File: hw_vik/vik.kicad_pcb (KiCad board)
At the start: 2 copper layers, 51.2 x 51.2 mm, 41 parts, among them J1 Conn_2Rows-05Pins, Q1 AO3401A, Q2 AO3401A, Q3 AO3401A, SW1 SW_DPST_x2, U1 PY32F002AF15P6TU

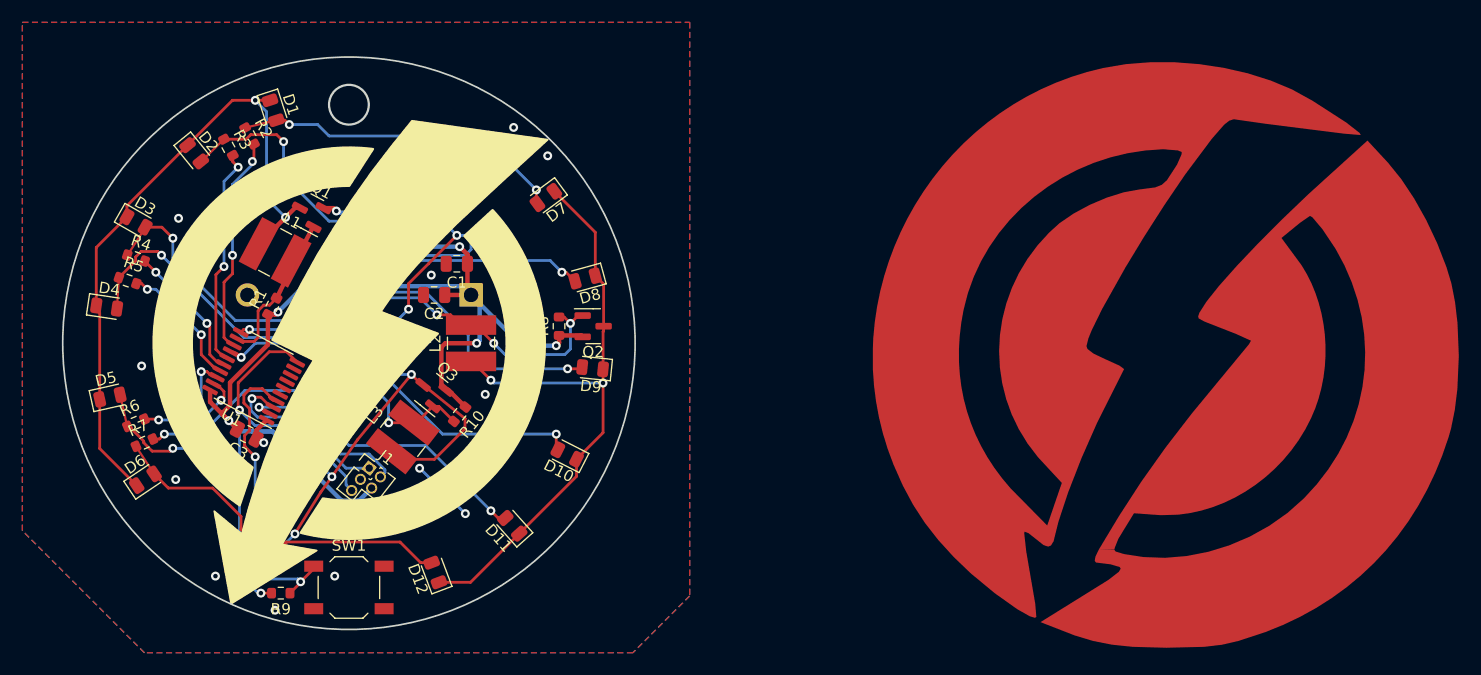
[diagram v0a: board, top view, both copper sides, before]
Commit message: Update pcb
Made FMask for exclude leds, added generated image
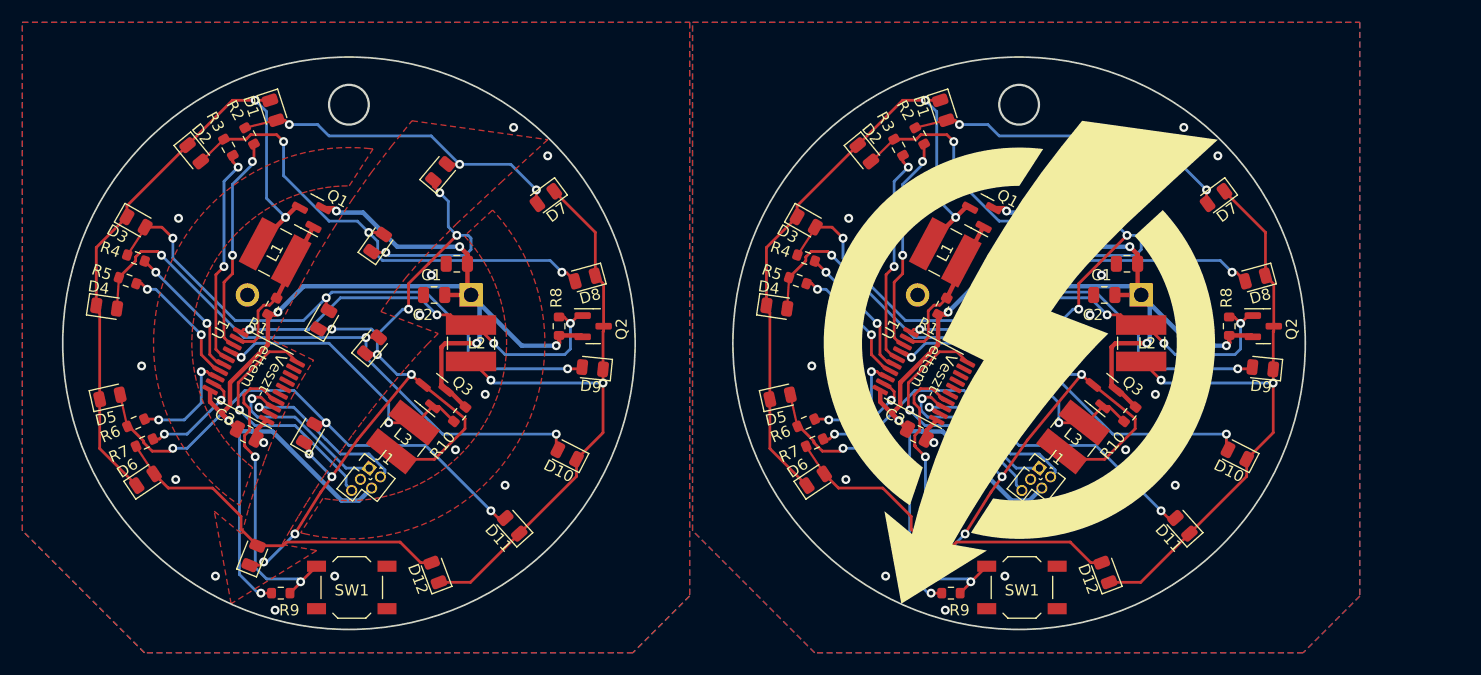
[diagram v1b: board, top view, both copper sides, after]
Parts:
- added BT1: CR2032, karifa:CR2032_Holder, B.Cu at (170.9, 95.7)
- added C1: 10uF, Capacitor_SMD:C_0805_2012Metric, F.Cu at (169.6, 92.9)
- added C2: 10uF, Capacitor_SMD:C_0805_2012Metric, F.Cu at (167.6, 95.7)
- added C3: 100nF, Capacitor_SMD:C_0805_2012Metric, F.Cu at (150.8, 108.1)
- added D1: LED, LED_SMD:LED_0805_2012Metric, F.Cu at (153.2, 79.2)
- added D10: LED, LED_SMD:LED_0805_2012Metric, F.Cu at (179.5, 110.0)
- added D11: LED, LED_SMD:LED_0805_2012Metric, F.Cu at (174.6, 116.3)
- added D12: LED, LED_SMD:LED_0805_2012Metric, F.Cu at (167.7, 120.5)
- added D13: LED, LED_SMD:LED_0805_2012Metric, F.Cu at (168.1, 84.7)
- added D14: LED, LED_SMD:LED_0805_2012Metric, F.Cu at (162.5, 91.0)
- added D15: LED, LED_SMD:LED_0805_2012Metric, F.Cu at (157.7, 97.9)
- added D16: LED, LED_SMD:LED_0805_2012Metric, F.Cu at (162.0, 100.2)
- added D17: LED, LED_SMD:LED_0805_2012Metric, F.Cu at (156.4, 108.1)
- added D18: LED, LED_SMD:LED_0805_2012Metric, F.Cu at (151.4, 119.0)
- added D2: LED, LED_SMD:LED_0805_2012Metric, F.Cu at (146.1, 83.0)
- added D3: LED, LED_SMD:LED_0805_2012Metric, F.Cu at (140.9, 89.2)
- added D4: LED, LED_SMD:LED_0805_2012Metric, F.Cu at (138.3, 96.8)
- added D5: LED, LED_SMD:LED_0805_2012Metric, F.Cu at (138.6, 104.8)
- added D6: LED, LED_SMD:LED_0805_2012Metric, F.Cu at (141.7, 112.2)
- added D7: LED, LED_SMD:LED_0805_2012Metric, F.Cu at (177.6, 87.0)
- added D8: LED, LED_SMD:LED_0805_2012Metric, F.Cu at (181.1, 94.2)
- added D9: LED, LED_SMD:LED_0805_2012Metric, F.Cu at (181.7, 102.2)
- added J1: Conn_2Rows-05Pins, karifa:ProgConnector_5pin, F.Cu at (161.8, 111.2)
- added L1: 1mH, Inductor_SMD:L_Ferrocore_DLG-0403, F.Cu at (153.3, 91.9)
- added L2: 1mH, Inductor_SMD:L_Ferrocore_DLG-0403, F.Cu at (170.9, 100.0)
- added L3: 1mH, Inductor_SMD:L_Ferrocore_DLG-0403, F.Cu at (164.8, 108.4)
- added Q1: AO3401A, karifa:SOT-23, F.Cu at (156.4, 88.3)
- added Q2: AO3401A, karifa:SOT-23, F.Cu at (181.8, 98.5)
- added Q3: AO3401A, karifa:SOT-23, F.Cu at (167.3, 104.3)
- added R1: 100k, Resistor_SMD:R_0603_1608Metric, F.Cu at (153.1, 96.7)
- added R10: 100k, Resistor_SMD:R_0603_1608Metric, F.Cu at (169.8, 106.3)
- added R2: 10, Resistor_SMD:R_0603_1608Metric, F.Cu at (151.1, 81.5)
- added R3: 10, Resistor_SMD:R_0603_1608Metric, F.Cu at (149.2, 82.5)
- added R4: 10, Resistor_SMD:R_0603_1608Metric, F.Cu at (140.9, 92.4)
- added R5: 10, Resistor_SMD:R_0603_1608Metric, F.Cu at (140.1, 94.4)
- added R6: 10, Resistor_SMD:R_0603_1608Metric, F.Cu at (140.9, 107.1)
- added R7: 10, Resistor_SMD:R_0603_1608Metric, F.Cu at (141.7, 108.9)
- added R8: 100k, Resistor_SMD:R_0603_1608Metric, F.Cu at (178.7, 98.5)
- added R9: 100k, Resistor_SMD:R_0603_1608Metric, F.Cu at (153.8, 122.4)
- added SW1: SW_DPST_x2, Button_Switch_SMD:SW_SPST_TL3342, F.Cu at (160.2, 121.8)
- added U1: PY32F002AF15P6TU, karifa:TSSOP-20_4.4x6.5mm_P0.65mm, F.Cu at (151.4, 102.9)
- moved SW1 0.25 mm to (100.3, 121.8)
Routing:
- net VCC: track 116.0 -> 232.0 mm, vias 7 -> 14
- net Net-(D1-K): track 61.0 -> 121.9 mm, vias 2 -> 4
- net Net-(D13-K): track 62.3 -> 122.8 mm, vias 11 -> 22
- net Net-(D10-K): track 57.2 -> 114.3 mm, vias 2 -> 4
- net Net-(D10-A): track 50.7 -> 101.4 mm, vias 3 -> 6
- net Net-(D15-A): track 49.8 -> 99.7 mm, vias 3 -> 6
- net Net-(D11-A): track 42.8 -> 85.7 mm, vias 3 -> 6
- net Net-(D14-A): track 40.9 -> 81.9 mm, vias 3 -> 6
- net /MPX2: track 38.0 -> 76.0 mm, vias 4 -> 8
- net Net-(D12-A): track 29.1 -> 58.1 mm
- net Net-(D1-A): track 28.3 -> 56.5 mm, vias 3 -> 6
- net Net-(SW1A-A): track 27.8 -> 55.7 mm, vias 2 -> 4
- net /MPX3: track 25.9 -> 51.8 mm, vias 2 -> 4
- net /nRST: track 22.8 -> 45.5 mm, vias 1 -> 2
- net /L2: track 19.7 -> 39.4 mm, vias 2 -> 4
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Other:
- board size 51.2 x 51.2 mm -> 111.1 x 51.2 mm
- board text added: "Veszt- ettem"
